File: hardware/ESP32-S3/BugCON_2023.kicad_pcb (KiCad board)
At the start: 2 copper layers, 31 parts, among them J1 Conn_01x04_Pin, J2 Conn_01x04_Pin, J4 Battery, P1 USB_C_Plug_USB2.0, Q1 DMG3415U-7, SW1 RESET, SW2 GPIO, SW3 ON, U1 ESP32-S3-WROOM-1U-N16, U2 AP2112K-3.3

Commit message: First_route_Change_size
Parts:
- removed the Ref** at (143.1, 78.9)
- added Ref**: Val**, FootprintsB:Bugcon_svg, F.Cu at (144.1, 73.0)
- moved SW2 107.3 mm to (198.5, 70.8)
- moved SW1 106.5 mm to (90.8, 70.5)
- moved R1 95.5 mm to (96.0, 71.0), turned to 90 degrees
- moved C7 25.9 mm to (131.9, 96.2), turned to 90 degrees
- moved C6 22.8 mm to (155.6, 93.6), turned to 90 degrees
- moved R2 3.63 mm to (113.7, 79.6), turned to -90 degrees
- moved C2 0.66 mm to (138.1, 98.8)
- moved C3 0.60 mm to (141.1, 98.8)
- moved C1 0.56 mm to (144.1, 98.8)
- moved R4 0.33 mm to (131.8, 41.6)
- moved SW3 0.26 mm to (144.0, 39.8)
- turned F1 to 90 degrees
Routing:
- net +3V3: track 0.00 -> 256.3 mm, vias 0 -> 2
- net /RST: track 0.00 -> 106.0 mm, vias 0 -> 2
- net /BOOT: track 0.00 -> 98.2 mm
- net /D+: track 0.00 -> 79.0 mm, vias 0 -> 2
- net /D-: track 0.00 -> 77.7 mm, vias 0 -> 2
- net /TX: track 0.00 -> 76.3 mm, vias 0 -> 1
- net /RX: track 0.00 -> 71.9 mm, vias 0 -> 1
- net /PIN: track 0.00 -> 65.0 mm, vias 0 -> 1
- net +3.3V: track 0.00 -> 63.1 mm
- net /SDA: track 0.00 -> 60.4 mm, vias 0 -> 1
- net +BATT: track 0.00 -> 58.2 mm
- net VBUS: track 0.00 -> 57.5 mm
- net /SCL: track 0.00 -> 46.3 mm, vias 0 -> 1
- net Net-(D2-DIN): track 0.00 -> 37.0 mm
- net Net-(D7-DOUT): track 0.00 -> 34.9 mm
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- added copper zone on B.Cu, net GND
- added copper zone on F.Cu, net GND
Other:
- board outline added: 122.4 x 97.9 mm

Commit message: Replace_connector
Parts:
- moved J1 73.8 mm to (179.3, 77.0)
- moved C5 0.92 mm to (135.7, 41.6)
- moved D8 0.82 mm to (163.4, 87.4)
- moved D2 0.82 mm to (124.0, 87.7)
- moved D7 0.63 mm to (150.6, 97.6)
- moved D6 0.47 mm to (137.0, 97.4)
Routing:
- net +3V3: track 256.3 -> 220.6 mm, vias 2 -> 3
- net /SCL: track 46.3 -> 62.9 mm
- net /SDA: track 60.4 -> 53.8 mm
- net GND: track 28.2 -> 23.3 mm, vias 11 -> 9
- net +3.3V: track 63.1 -> 67.8 mm
- net Net-(F1-Pad1): track 17.2 -> 15.1 mm
- net Net-(D7-DOUT): track 34.9 -> 33.4 mm
- net /TX: track 76.3 -> 75.7 mm
- net /RX: track 71.9 -> 71.4 mm
- net Net-(D6-DIN): track 4.42 -> 4.92 mm

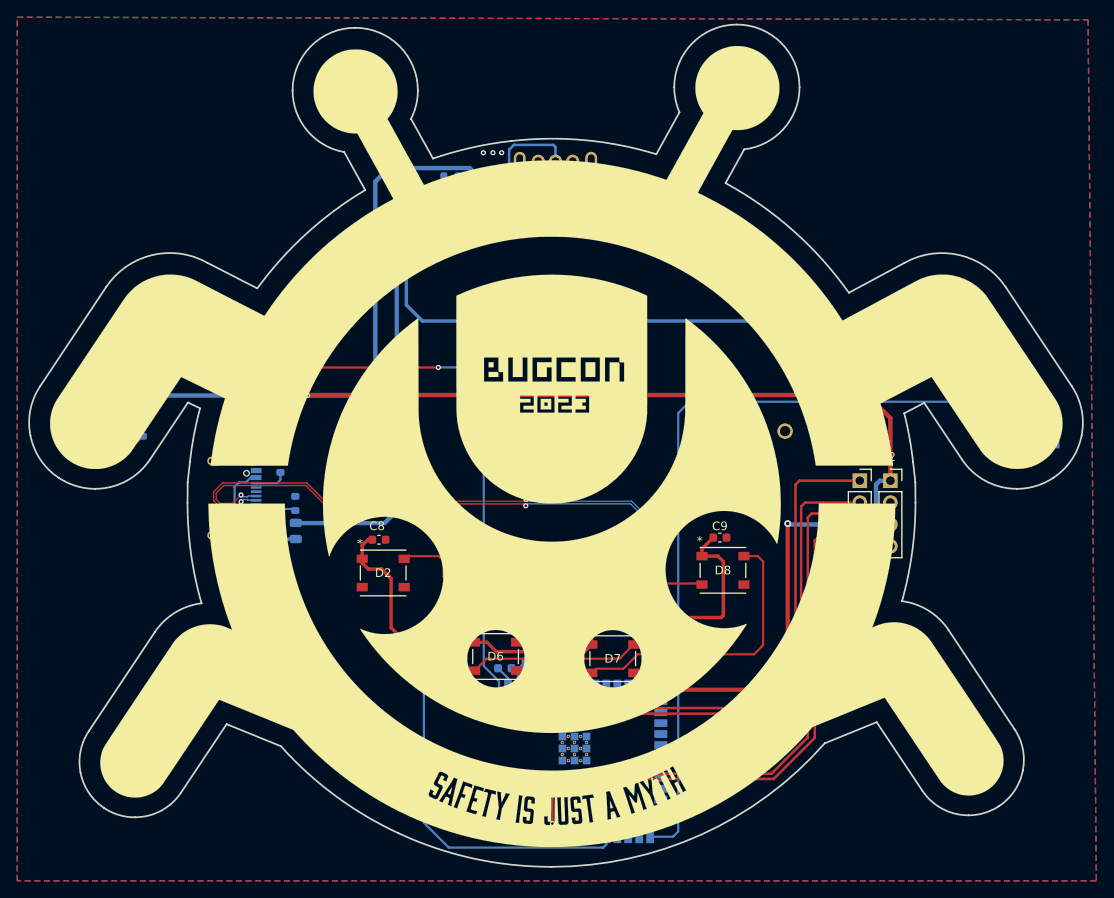
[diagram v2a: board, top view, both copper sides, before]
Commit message: Change Place_OLED
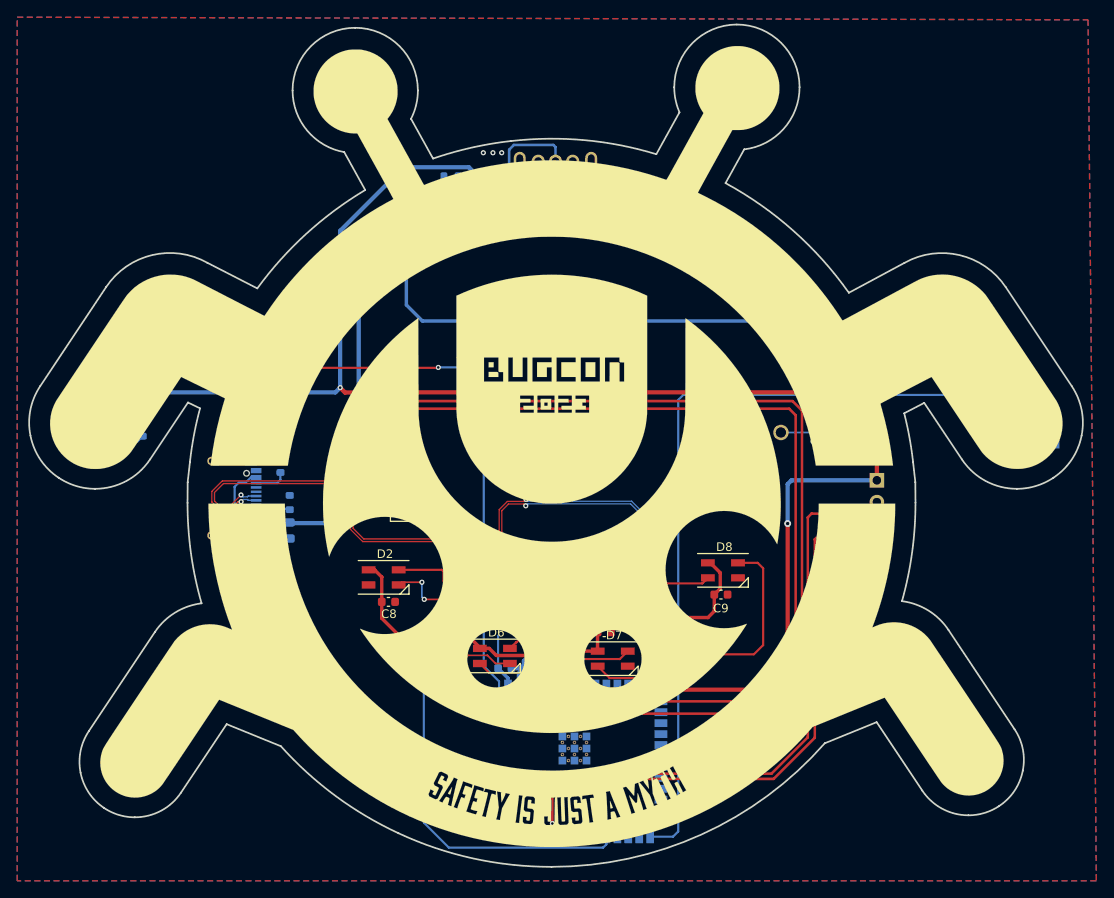
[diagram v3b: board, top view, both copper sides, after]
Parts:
- removed J4: Battery, FootprintsB:BAT_12BH331P-GR
- added J3: Conn_01x02, FootprintsB:BAT_12BH331P-GR, B.Cu at (143.5, 73.6)
- added kibuzzard-6515D6F9: G***, kibuzzard-6515D6F9, B.Cu at (129.6, 72.7)
- added kibuzzard-6515D70B: G***, kibuzzard-6515D70B, B.Cu at (129.4, 75.2)
- added kibuzzard-6515D74A: G***, kibuzzard-6515D74A, B.Cu at (184.4, 79.5)
- added kibuzzard-6515D75F: G***, kibuzzard-6515D75F, B.Cu at (184.5, 82.1)
- added kibuzzard-6515D795: G***, kibuzzard-6515D795, B.Cu at (181.4, 87.3)
- added kibuzzard-6515D795: G***, kibuzzard-6515D795, B.Cu at (129.7, 80.4)
- added kibuzzard-6515D7CD: G***, kibuzzard-6515D7CD, B.Cu at (129.1, 77.9)
- added kibuzzard-6515D7CD: G***, kibuzzard-6515D7CD, B.Cu at (184.4, 76.9)
- D2, D6, D7, D8: footprint FootprintsB:WS2812B_WDS -> FootprintsB:LED_SK6812MINI_PLCC4_3.5x3.5mm_P1.75mm
- J2: moved to B.Cu
- moved J1 53.4 mm to (126.1, 72.7)
- moved C8 7.30 mm to (124.6, 91.0)
- moved C9 6.63 mm to (163.2, 90.2)
- moved C6 6.05 mm to (149.6, 94.6), turned to 180 degrees
- moved J2 1.58 mm to (181.3, 76.9), turned to 180 degrees
- moved C7 1.48 mm to (133.3, 96.4)
- moved F1 0.81 mm to (113.0, 82.8)
- moved R2 0.66 mm to (113.1, 79.5)
- moved D2 0.51 mm to (124.0, 88.2)
- moved D6 0.10 mm to (136.9, 97.3)
- turned SW2 to 0 degrees
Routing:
- net /SCL: track 62.9 -> 126.0 mm
- net /SDA: track 53.8 -> 103.4 mm
- net GND: track 23.3 -> 51.1 mm, vias 9 -> 18
- net +3.3V: track 67.8 -> 58.2 mm
- net /D+: track 79.0 -> 87.3 mm
- net /D-: track 77.7 -> 86.0 mm
- net +3V3: track 220.6 -> 227.2 mm
- net VBUS: track 57.5 -> 55.6 mm
- net /TX: track 75.7 -> 74.1 mm
- net /RX: track 71.4 -> 69.9 mm
- net Net-(D6-DOUT): track 19.8 -> 18.7 mm
- net Net-(D6-DIN): track 4.92 -> 5.98 mm
- net Net-(F1-Pad1): track 15.1 -> 14.3 mm
- net Net-(P1-CC): track 4.62 -> 3.93 mm

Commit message: Add_Hole
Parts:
- added REF**: MountingHole_3.2mm_M3_ISO14580, MountingHole:MountingHole_3.2mm_M3_ISO14580, F.Cu at (143.6, 43.7)
- moved C2 23.1 mm to (147.0, 120.1), turned to 0 degrees
- moved SW3 22.7 mm to (121.6, 36.1), turned to 120 degrees
- moved C3 21.3 mm to (141.0, 120.1), turned to 180 degrees
- moved C1 21.3 mm to (144.0, 120.1), turned to 180 degrees
- moved U1 1.34 mm to (144.4, 108.5), turned to 90 degrees
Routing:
- net /PIN: track 64.9 -> 15.5 mm
- net GND: track 51.1 -> 98.3 mm, vias 18 -> 29
- net /SDA: track 103.4 -> 141.3 mm
- net /RST: track 106.2 -> 131.3 mm, vias 2 -> 4
- net /TX: track 74.1 -> 54.6 mm, vias 1 -> 0
- net /BOOT: track 98.1 -> 116.5 mm
- net /D+: track 87.3 -> 76.1 mm
- net /D-: track 86.0 -> 75.8 mm
- net /RX: track 69.9 -> 60.8 mm, vias 1 -> 0
- net Net-(SW3-B): track 18.1 -> 27.2 mm, vias 0 -> 1
- net /SCL: track 126.0 -> 134.8 mm
- net +3V3: track 227.2 -> 235.8 mm
- net Net-(D7-DOUT): track 33.5 -> 32.7 mm
- net Net-(D1-K): track 21.8 -> 22.1 mm, vias 0 -> 1

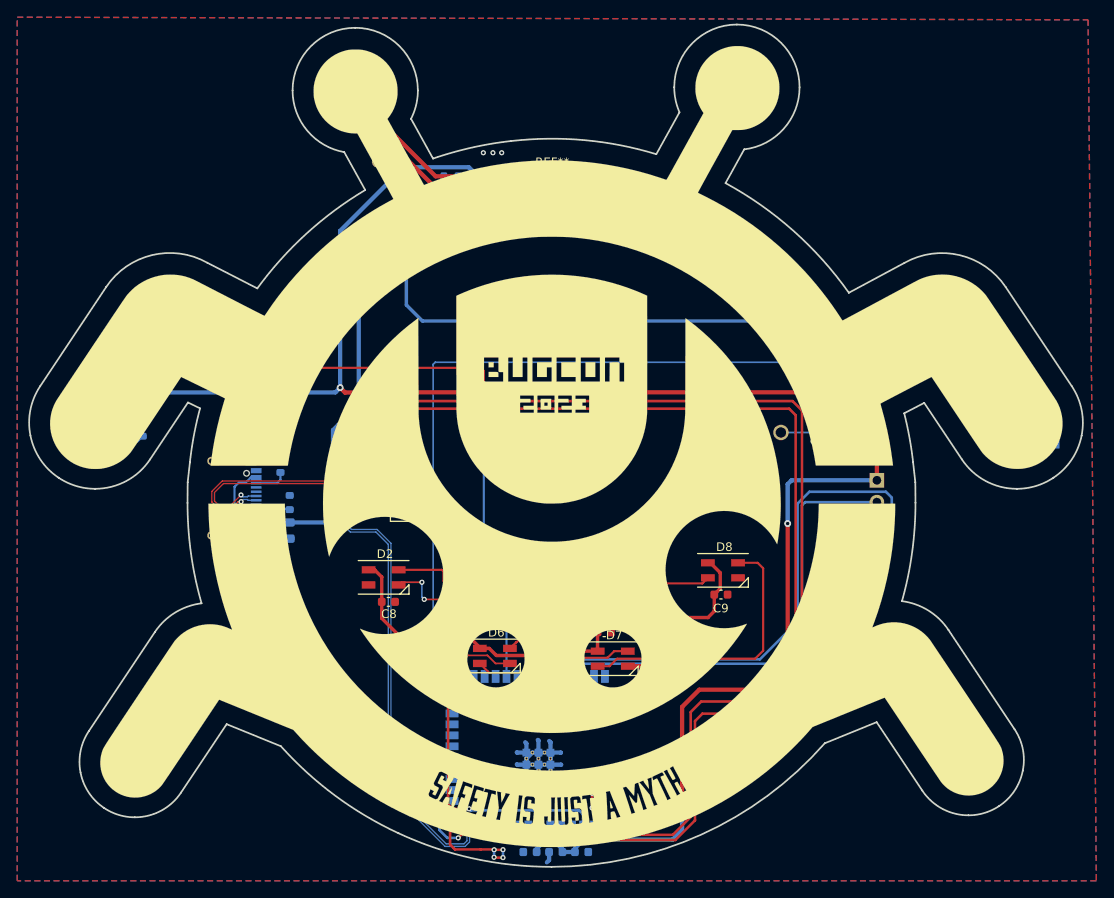
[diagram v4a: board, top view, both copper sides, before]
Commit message: fix usb traces & add 3d models
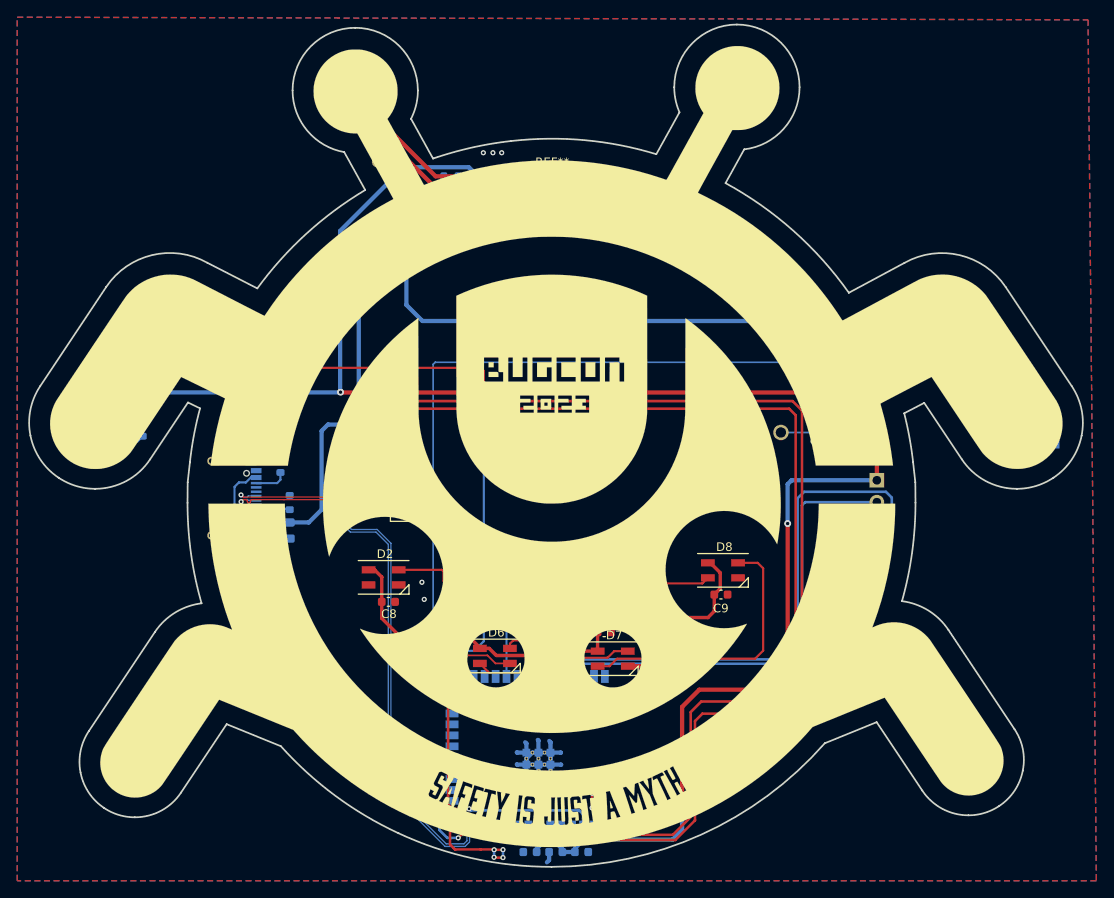
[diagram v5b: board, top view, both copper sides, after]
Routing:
- net /D+: track 76.1 -> 68.8 mm
- net GND: track 98.3 -> 91.3 mm
- net /D-: track 75.8 -> 68.9 mm
- net /RST: track 131.3 -> 133.1 mm
- net /RX: track 60.8 -> 62.6 mm
- net +3V3: track 235.8 -> 234.9 mm

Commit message: Update_PCB
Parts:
- added J4: Conn_01x01_Pin, Connector_PinHeader_1.00mm:PinHeader_1x01_P1.00mm_Horizontal, F.Cu at (95.0, 109.8)
- added J5: Conn_01x01_Pin, Connector_PinHeader_1.00mm:PinHeader_1x01_P1.00mm_Horizontal, F.Cu at (191.8, 109.4)
- U1: value ESP32-S3-WROOM-1U-N16 -> ESP32-S3-WROOM-1-N4
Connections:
- U1 pad 11: unconnected-(U1-IO18-Pad11) -> /TCH2
- U1 pad 7: unconnected-(U1-IO7-Pad7) -> /TCH1
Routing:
- net /TCH1: track 0.00 -> 82.0 mm, vias 0 -> 1
- net /TCH2: track 0.00 -> 60.9 mm, vias 0 -> 1
- net GND: track 91.3 -> 101.4 mm
- net +3V3: track 234.9 -> 236.2 mm
- net /SDA: track 141.3 -> 141.9 mm

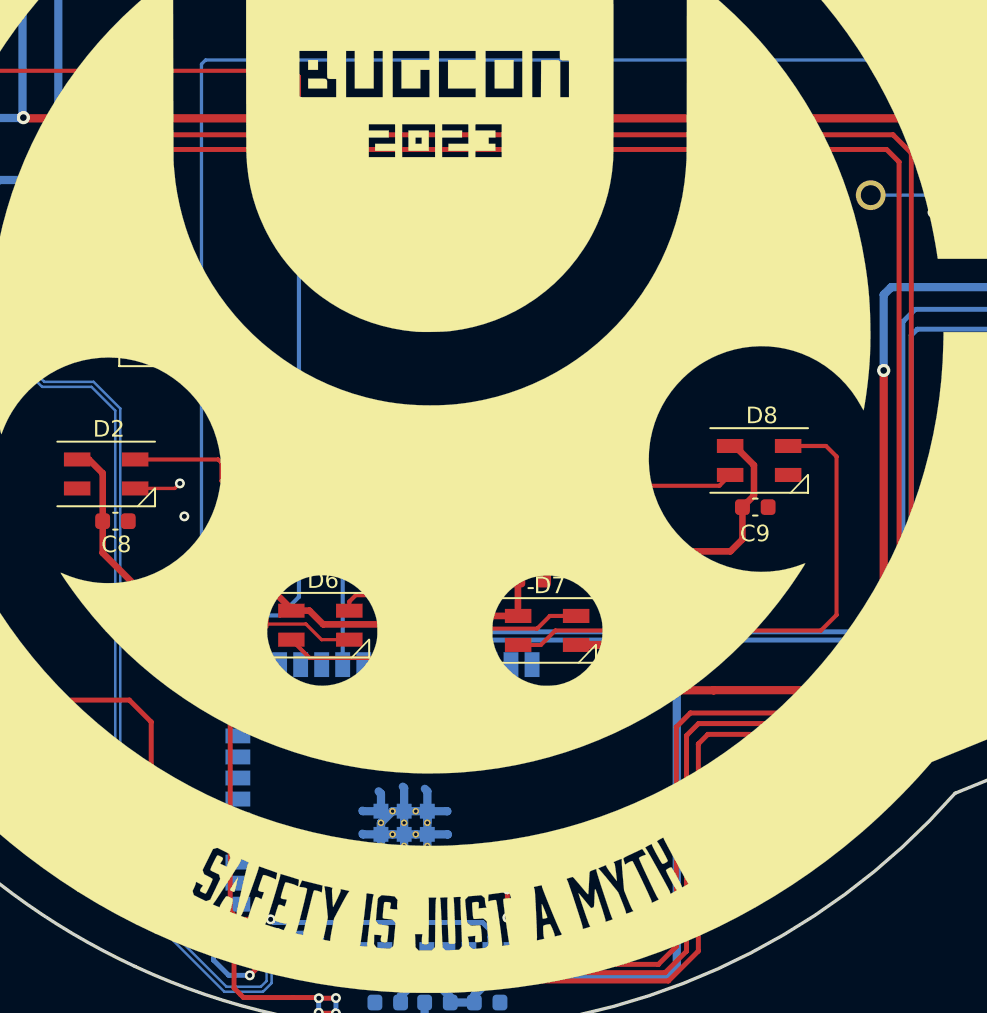
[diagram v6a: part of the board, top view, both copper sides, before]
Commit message: fix 3.3v label on esp32 badge
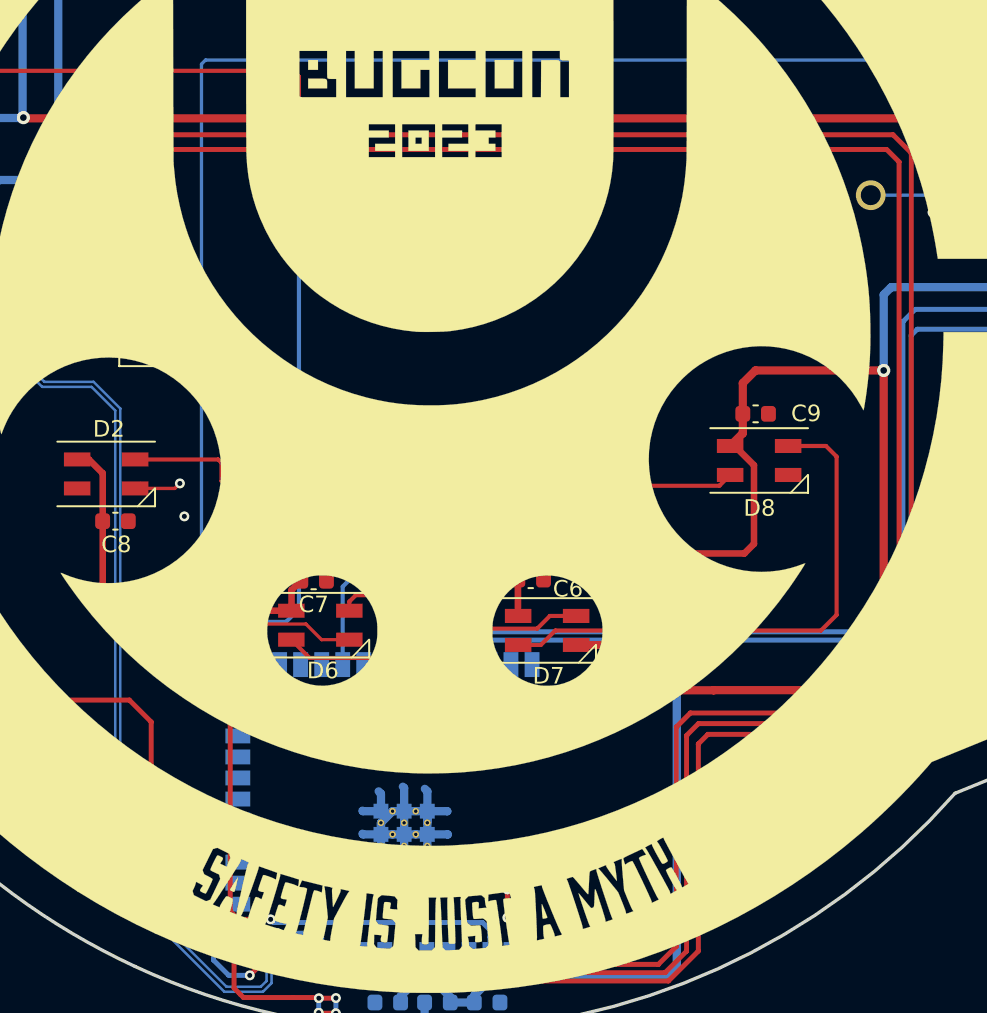
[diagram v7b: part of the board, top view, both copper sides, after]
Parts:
- moved C9 5.63 mm to (163.2, 84.6)
- moved C7 3.62 mm to (136.5, 94.6), turned to 180 degrees
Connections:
- C6 pad 2: +3.3V -> +3V3
- C7 pad 2: +3.3V -> +3V3
- C8 pad 2: +3.3V -> +3V3
- C9 pad 2: +3.3V -> +3V3
- D2 pad 1: +3.3V -> +3V3
- D6 pad 1: +3.3V -> +3V3
- D7 pad 1: +3.3V -> +3V3
- D8 pad 1: +3.3V -> +3V3
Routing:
- net +3V3: track 236.2 -> 311.6 mm
- net +3.3V: track 58.2 -> 0.00 mm
- net /PIN: track 15.5 -> 13.5 mm

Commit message: Replace_serial_conn
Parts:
- removed kibuzzard-6515D74A: G***, kibuzzard-6515D74A
- removed kibuzzard-6515D75F: G***, kibuzzard-6515D75F
- removed the kibuzzard-6515D7CD at (184.4, 76.9)
- added kibuzzard-652D8C83: G***, kibuzzard-652D8C83, B.Cu at (191.2, 58.4)
- added kibuzzard-652D8C8F: G***, kibuzzard-652D8C8F, B.Cu at (192.6, 60.4)
- added kibuzzard-652D8CA2: G***, kibuzzard-652D8CA2, B.Cu at (194.2, 62.5)
- moved kibuzzard-6515D795 27.1 mm to (195.7, 64.4), turned to -145 degrees
- moved J2 24.5 mm to (194.3, 56.1), turned to -145 degrees
- moved SW2 19.0 mm to (179.6, 72.2), turned to 90 degrees
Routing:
- net /TX: track 54.6 -> 85.3 mm
- net /RX: track 62.6 -> 91.2 mm
- net /BOOT: track 116.5 -> 99.2 mm
- net +3V3: track 311.6 -> 304.3 mm, vias 3 -> 2
- net GND: track 101.4 -> 104.5 mm
